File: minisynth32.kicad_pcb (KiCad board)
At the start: 2 copper layers, 49.5 x 97.8 mm, 22 parts, among them J1 F_PANEL, J2 Conn_02x20_Odd_Even, J3 PJ-002A, J4 ROT_HDR, J5 MIDI_IN, J6 R_BREAKOUT, J7 SSD1306 OLED, SW1 B1, SW2 PB400EEQR1BLK, SW3 B2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

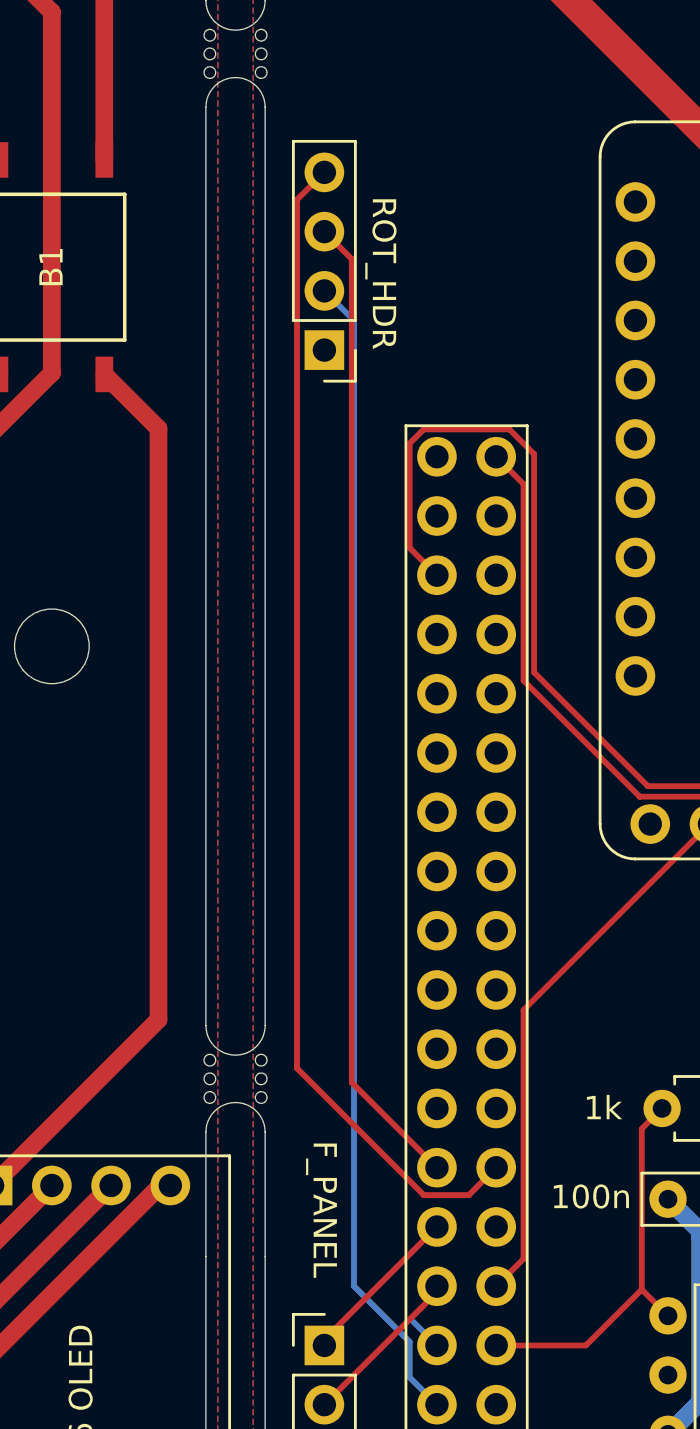
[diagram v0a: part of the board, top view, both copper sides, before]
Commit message: Move ROT_HDR for RPi 3B
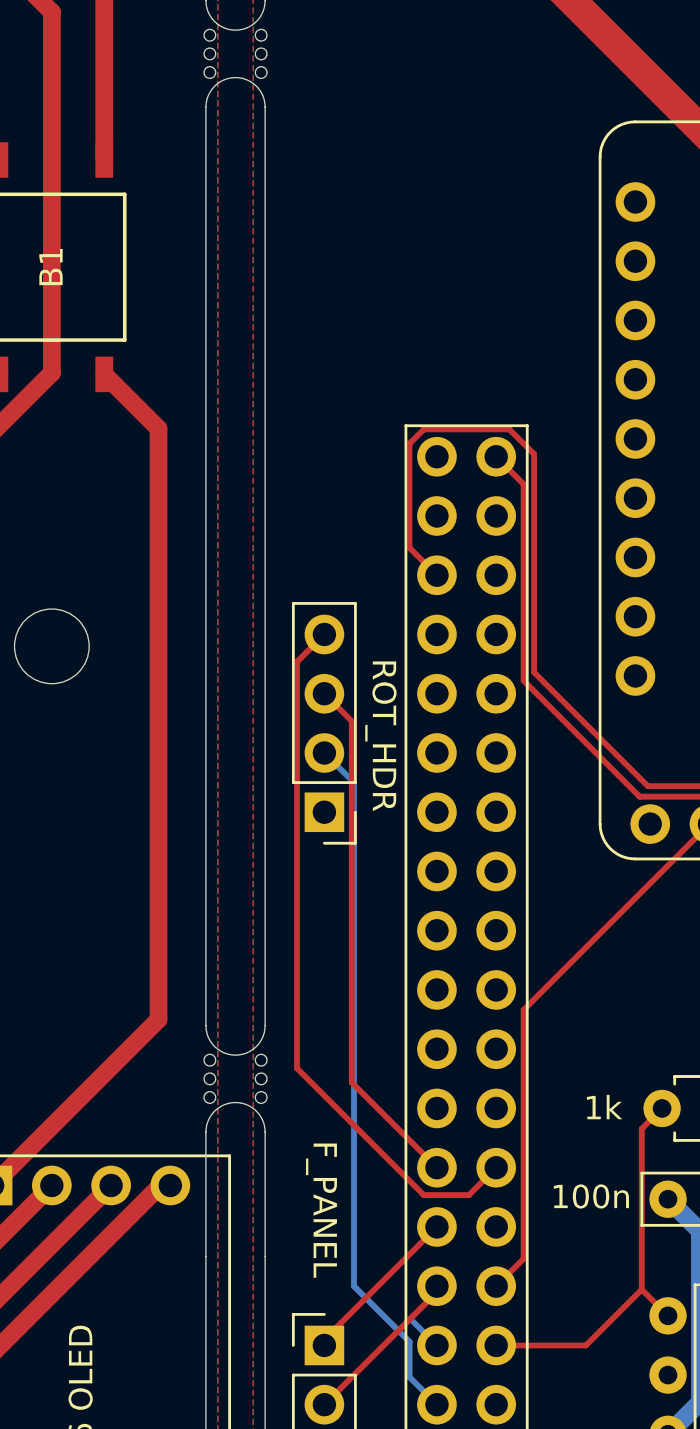
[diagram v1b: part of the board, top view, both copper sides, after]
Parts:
- moved J4 19.8 mm to (132.1, 103.6)
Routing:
- net ENC_BTN: track 50.0 -> 29.9 mm
- net ENC_DAT: track 50.4 -> 30.4 mm
- net ENC_CLK: track 42.1 -> 22.3 mm

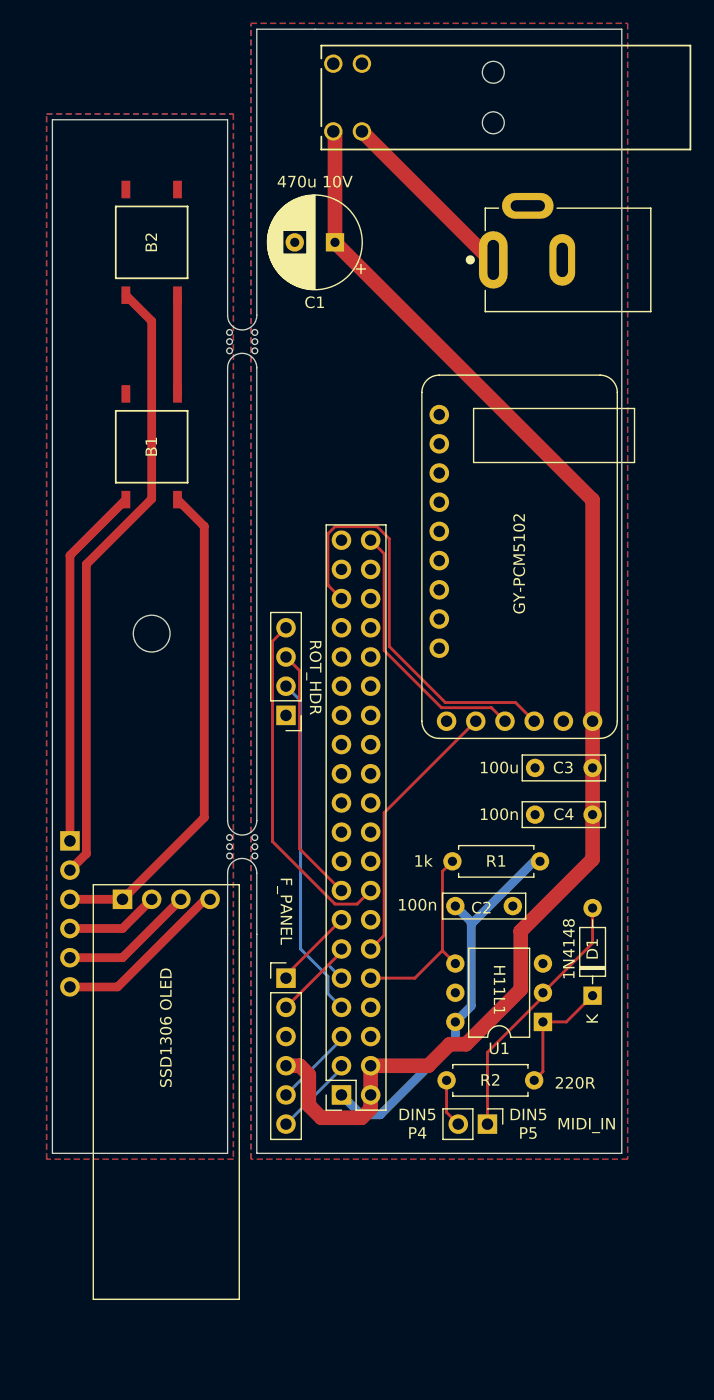
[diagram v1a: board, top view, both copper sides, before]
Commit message: PCB rev 1.1 (rear only): cutaway to support RPi3B
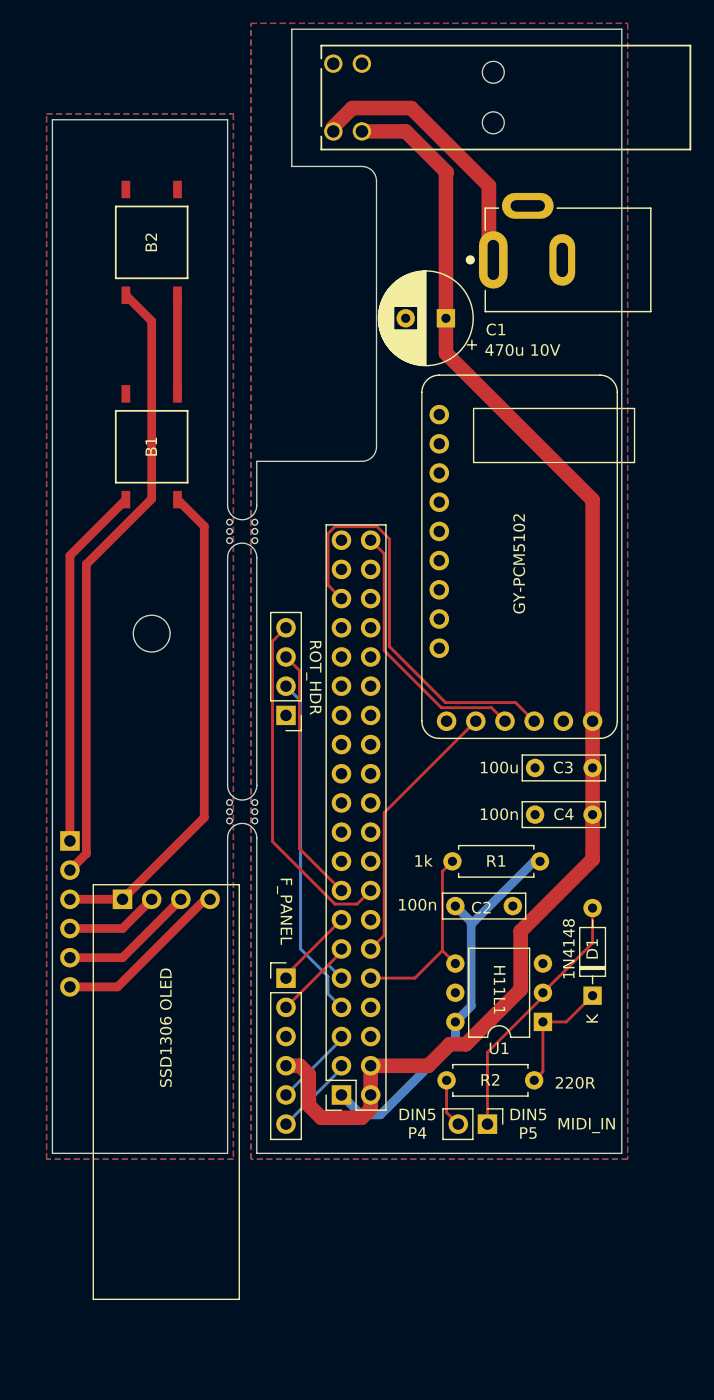
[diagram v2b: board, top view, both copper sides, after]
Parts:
- moved mouse-bite-2.54mm-slot 16.5 mm to (128.3, 87.6)
- moved C1 11.7 mm to (146.0, 69.1)
- moved mouse-bite-2.54mm-slot 3.05 mm to (128.3, 112.0)
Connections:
- SW2 pad 1: +5V -> Net-(J3-Pad1)
- SW2 pad 2: Net-(J3-Pad1) -> +5V
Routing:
- net Net-(J3-Pad1): track 16.1 -> 24.5 mm
- net +5V: track 117.5 -> 118.7 mm
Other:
- outline, holes or cut-outs redrawn
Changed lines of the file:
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@@
   (general
     (thickness 1.6)
-    (drawings 71)
-    (tracks 108)
+    (drawings 74)
+    (tracks 117)
     (zones 0)
     (modules 22)
@@
   (title_block
     (title "Minisynth 32: Rear panel breakout and front panel board")
-    (rev 1.0)
+    (rev 1.1)
     (company https://github.com/grantek/minisynth32)
     (comment 1 "ClumsyMIDI footprints (c) Andreas Zdziarstek")
@@
     (visible_elements FFFFFF7F)
     (pcbplotparams
-      (layerselection 0x010fc_ffffffff)
-      (usegerberextensions false)
+      (layerselection 0x010f0_ffffffff)
+      (usegerberextensions true)
       (usegerberattributes true)
       (usegerberadvancedattributes true)
@@
       (outputformat 1)
       (mirror false)
-      (drillshape 1)
+      (drillshape 0)
       (scaleselection 1)
-      (outputdirectory ""))
+      (outputdirectory "gerber/front_rear"))
   )
   (net 0 "")
@@
       (net 48 "Net-(SW2-Pad3)"))
     (pad 2 thru_hole circle (at 0 2.4892 90) (size 1.6002 1.6002) (drill 1.0922) (layers *.Cu *.Mask)
+      (net 1 +5V))
+    (pad 1 thru_hole circle (at 0 0 90) (size 1.6002 1.6002) (drill 1.0922) (layers *.Cu *.Mask)
       (net 44 "Net-(J3-Pad1)"))
-    (pad 1 thru_hole circle (at 0 0 90) (size 1.6002 1.6002) (drill 1.0922) (layers *.Cu *.Mask)
-      (net 1 +5V))
   )
   (module minisynth32:TL3301AF160QG-nopaste (layer F.Cu)
@@
   )
   (module minisynth32:mouse-bite-2.54mm-slot (layer F.Cu)
-    (at 128.27 115.062 90)
+    (at 128.27 112.014 90)
     (fp_text reference mouse-bite-2.54mm-slot (at 0 -2 90) (layer F.SilkS) hide
       (effects (font (size 1 1) (thickness 0.2)))
@@
   )
   (module minisynth32:mouse-bite-2.54mm-slot (layer F.Cu)
-    (at 128.27 71.12 90)
+    (at 128.27 87.63 90)
     (fp_text reference mouse-bite-2.54mm-slot (at 0 -2 90) (layer F.SilkS) hide
       (effects (font (size 1 1) (thickness 0.2)))
@@
   )
   (module Capacitor_THT:CP_Radial_D8.0mm_P3.50mm (layer F.Cu)
-    (at 136.342 62.484 180)
+    (at 145.994 69.088 180)
     (descr "CP, Radial series, Radial, pin pitch=3.50mm, , diameter=8mm, Electrolytic Capacitor")
     (tags "CP Radial series Radial pin pitch 3.50mm  diameter 8mm Electrolytic Capacitor")
-    (fp_text reference C1 (at 1.75 -5.25) (layer F.SilkS)
-      (effects (font (size 1 1) (thickness 0.15)))
-    )
-    (fp_text value "470u 10V" (at 1.75 5.25) (layer F.SilkS)
+    (fp_text reference C1 (at -4.374 -1.016) (layer F.SilkS)
+      (effects (font (size 1 1) (thickness 0.15)))
+    )
+    (fp_text value "470u 10V" (at -6.66 -2.794) (layer F.SilkS)
       (effects (font (size 1 1) (thickness 0.15)))
     )
@@
     )
   )
+  (gr_arc (start 128.27 85.344) (end 127 85.344) (angle -180) (layer Edge.Cuts) (width 0.05))
+  (gr_arc (start 128.27 89.916) (end 129.54 89.916) (angle -180) (layer Edge.Cuts) (width 0.05))
+  (gr_arc (start 128.27 109.728) (end 127 109.728) (angle -180) (layer Edge.Cuts) (width 0.05))
+  (gr_arc (start 128.27 114.3) (end 129.54 114.3) (angle -180) (layer Edge.Cuts) (width 0.05))
+  (gr_line (start 129.54 114.3) (end 129.54 141.732) (layer Edge.Cuts) (width 0.05))
+  (gr_line (start 127 141.732) (end 127 114.3) (layer Edge.Cuts) (width 0.05))
+  (gr_line (start 127 109.728) (end 127 89.916) (layer Edge.Cuts) (width 0.05))
+  (gr_line (start 129.54 89.916) (end 129.54 109.728) (layer Edge.Cuts) (width 0.05))
+  (gr_line (start 132.588 55.88) (end 132.588 43.942) (layer Edge.Cuts) (width 0.05))
+  (gr_line (start 129.54 85.344) (end 129.54 81.534) (layer Edge.Cuts) (width 0.05))
+  (gr_line (start 127 51.816) (end 127 85.344) (layer Edge.Cuts) (width 0.05))
+  (gr_line (start 139.954 80.264) (end 139.954 57.15) (layer Edge.Cuts) (width 0.05))
+  (gr_arc (start 138.684 57.15) (end 139.954 57.15) (angle -90) (layer Edge.Cuts) (width 0.05))
+  (gr_line (start 138.684 81.534) (end 129.54 81.534) (layer Edge.Cuts) (width 0.05))
+  (gr_arc (start 138.684 80.264) (end 138.684 81.534) (angle -90) (layer Edge.Cuts) (width 0.05))
+  (gr_line (start 138.684 55.88) (end 132.588 55.88) (layer Edge.Cuts) (width 0.05))
   (gr_text "Minisynth 32: Rear panel breakout board\nhttps://github.com/grantek/minisynth32" (at 158.242 99.822 -90) (layer B.SilkS)
     (effects (font (size 1 1) (thickness 0.15)) (justify left mirror))
@@
     (effects (font (size 1 1) (thickness 0.15)) (justify mirror))
   )
-  (gr_line (start 129.54 73.406) (end 129.54 112.776) (layer Edge.Cuts) (width 0.05))
-  (gr_line (start 127 112.776) (end 127 73.406) (layer Edge.Cuts) (width 0.05))
-  (gr_line (start 129.54 117.348) (end 129.54 122.682) (layer Edge.Cuts) (width 0.05))
-  (gr_line (start 127 122.682) (end 127 117.348) (layer Edge.Cuts) (width 0.05))
-  (gr_arc (start 128.27 117.348) (end 129.54 117.348) (angle -180) (layer Edge.Cuts) (width 0.05))
-  (gr_arc (start 128.27 112.776) (end 127 112.776) (angle -180) (layer Edge.Cuts) (width 0.05))
   (gr_line (start 121.666 119.634) (end 119.634 119.634) (layer Dwgs.User) (width 0.15))
   (gr_line (start 119.38 62.484) (end 121.92 62.484) (layer Dwgs.User) (width 0.15))
   (gr_line (start 119.38 80.264) (end 121.92 80.264) (layer Dwgs.User) (width 0.15))
-  (gr_line (start 127 122.682) (end 127 141.732) (layer Edge.Cuts) (width 0.05))
-  (gr_line (start 127 51.816) (end 127 68.834) (layer Edge.Cuts) (width 0.05))
-  (gr_line (start 129.54 122.682) (end 129.54 141.732) (layer Edge.Cuts) (width 0.05))
-  (gr_line (start 129.54 43.942) (end 129.54 68.834) (layer Edge.Cuts) (width 0.05))
-  (gr_arc (start 128.27 68.834) (end 127 68.834) (angle -180) (layer Edge.Cuts) (width 0.05))
-  (gr_arc (start 128.27 73.406) (end 129.54 73.406) (angle -180) (layer Edge.Cuts) (width 0.05))
   (gr_line (start 121.412 96.52) (end 119.38 96.52) (layer Dwgs.User) (width 0.15))
   (gr_line (start 111.76 51.308) (end 127 51.308) (layer Dwgs.User) (width 0.15))
@@
     (effects (font (size 1 1) (thickness 0.15)))
   )
-  (gr_line (start 134.62 43.942) (end 129.54 43.942) (layer Edge.Cuts) (width 0.05))
-  (gr_line (start 161.29 43.942) (end 134.62 43.942) (layer Edge.Cuts) (width 0.05))
+  (gr_line (start 161.29 43.942) (end 132.588 43.942) (layer Edge.Cuts) (width 0.05))
   (gr_line (start 161.29 141.732) (end 161.29 43.942) (layer Edge.Cuts) (width 0.05))
   (gr_line (start 134.62 141.732) (end 161.29 141.732) (layer Edge.Cuts) (width 0.05))
@@
   (segment (start 158.75 112.268) (end 158.75 108.204) (width 1.27) (layer F.Cu) (net 1) (status 30))
   (segment (start 158.75 108.204) (end 158.75 104.14) (width 1.27) (layer F.Cu) (net 1) (status 30))
-  (segment (start 158.75 84.892) (end 136.342 62.484) (width 1.27) (layer F.Cu) (net 1) (status 20))
   (segment (start 158.75 104.14) (end 158.75 84.892) (width 1.27) (layer F.Cu) (net 1) (status 10))
-  (segment (start 136.342 52.9792) (end 136.1948 52.832) (width 1.27) (layer F.Cu) (net 1) (status 30))
-  (segment (start 136.342 62.484) (end 136.342 52.9792) (width 1.27) (layer F.Cu) (net 1) (status 30))
   (segment (start 132.08 134.112) (end 131.826 134.112) (width 0.25) (layer F.Cu) (net 1) (status 30))
   (segment (start 133.282081 134.112) (end 132.08 134.112) (width 1.27) (layer F.Cu) (net 1) (status 20))
@@
   (segment (start 139.446 137.855002) (end 138.664001 138.637001) (width 1.27) (layer F.Cu) (net 1))
   (segment (start 139.446 136.652) (end 139.446 137.855002) (width 1.27) (layer F.Cu) (net 1) (status 10))
+  (segment (start 145.994 72.136) (end 158.75 84.892) (width 1.27) (layer F.Cu) (net 1))
+  (segment (start 145.994 69.088) (end 145.994 72.136) (width 1.27) (layer F.Cu) (net 1))
+  (segment (start 138.684 52.832) (end 142.494 52.832) (width 1.27) (layer F.Cu) (net 1))
+  (segment (start 142.494 52.832) (end 146.05 56.388) (width 1.27) (layer F.Cu) (net 1))
+  (segment (start 145.994 56.444) (end 145.994 69.088) (width 1.27) (layer F.Cu) (net 1))
+  (segment (start 146.05 56.388) (end 145.994 56.444) (width 1.27) (layer F.Cu) (net 1))
   (segment (start 136.906 126.492) (end 135.89 125.476) (width 0.25) (layer B.Cu) (net 2))
   (segment (start 135.730999 87.827999) (end 135.730999 92.296999) (width 0.25) (layer F.Cu) (net 3))
@@
   (segment (start 133.35 102.362) (end 132.08 101.092) (width 0.25) (layer B.Cu) (net 42))
   (segment (start 133.35 123.952) (end 133.35 102.362) (width 0.25) (layer B.Cu) (net 42))
+  (segment (start 136.342 52.9792) (end 136.1948 52.832) (width 1.27) (layer F.Cu) (net 44) (status 30))
   (segment (start 149.86 64.008) (end 150.114 64.008) (width 1.27) (layer F.Cu) (net 44) (status 30))
-  (segment (start 138.684 52.832) (end 149.86 64.008) (width 1.27) (layer F.Cu) (net 44) (status 30))
+  (segment (start 149.72899 63.62299) (end 150.114 64.008) (width 1.27) (layer F.Cu) (net 44))
+  (segment (start 149.72899 57.563818) (end 149.72899 63.62299) (width 1.27) (layer F.Cu) (net 44))
+  (segment (start 142.965172 50.8) (end 149.72899 57.563818) (width 1.27) (layer F.Cu) (net 44))
+  (segment (start 137.85205 50.8) (end 142.965172 50.8) (width 1.27) (layer F.Cu) (net 44))
+  (segment (start 136.1948 52.45725) (end 137.85205 50.8) (width 1.27) (layer F.Cu) (net 44))
+  (segment (start 136.1948 52.832) (end 136.1948 52.45725) (width 1.27) (layer F.Cu) (net 44))
   (segment (start 146.05 138.176) (end 147.066 139.192) (width 0.25) (layer F.Cu) (net 45) (status 20))
   (segment (start 146.05 135.382) (end 146.05 138.176) (width 0.25) (layer F.Cu) (net 45) (status 10))
